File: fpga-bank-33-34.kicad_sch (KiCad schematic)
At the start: 1 part, among them U1 XC7K410T-2FFG900I

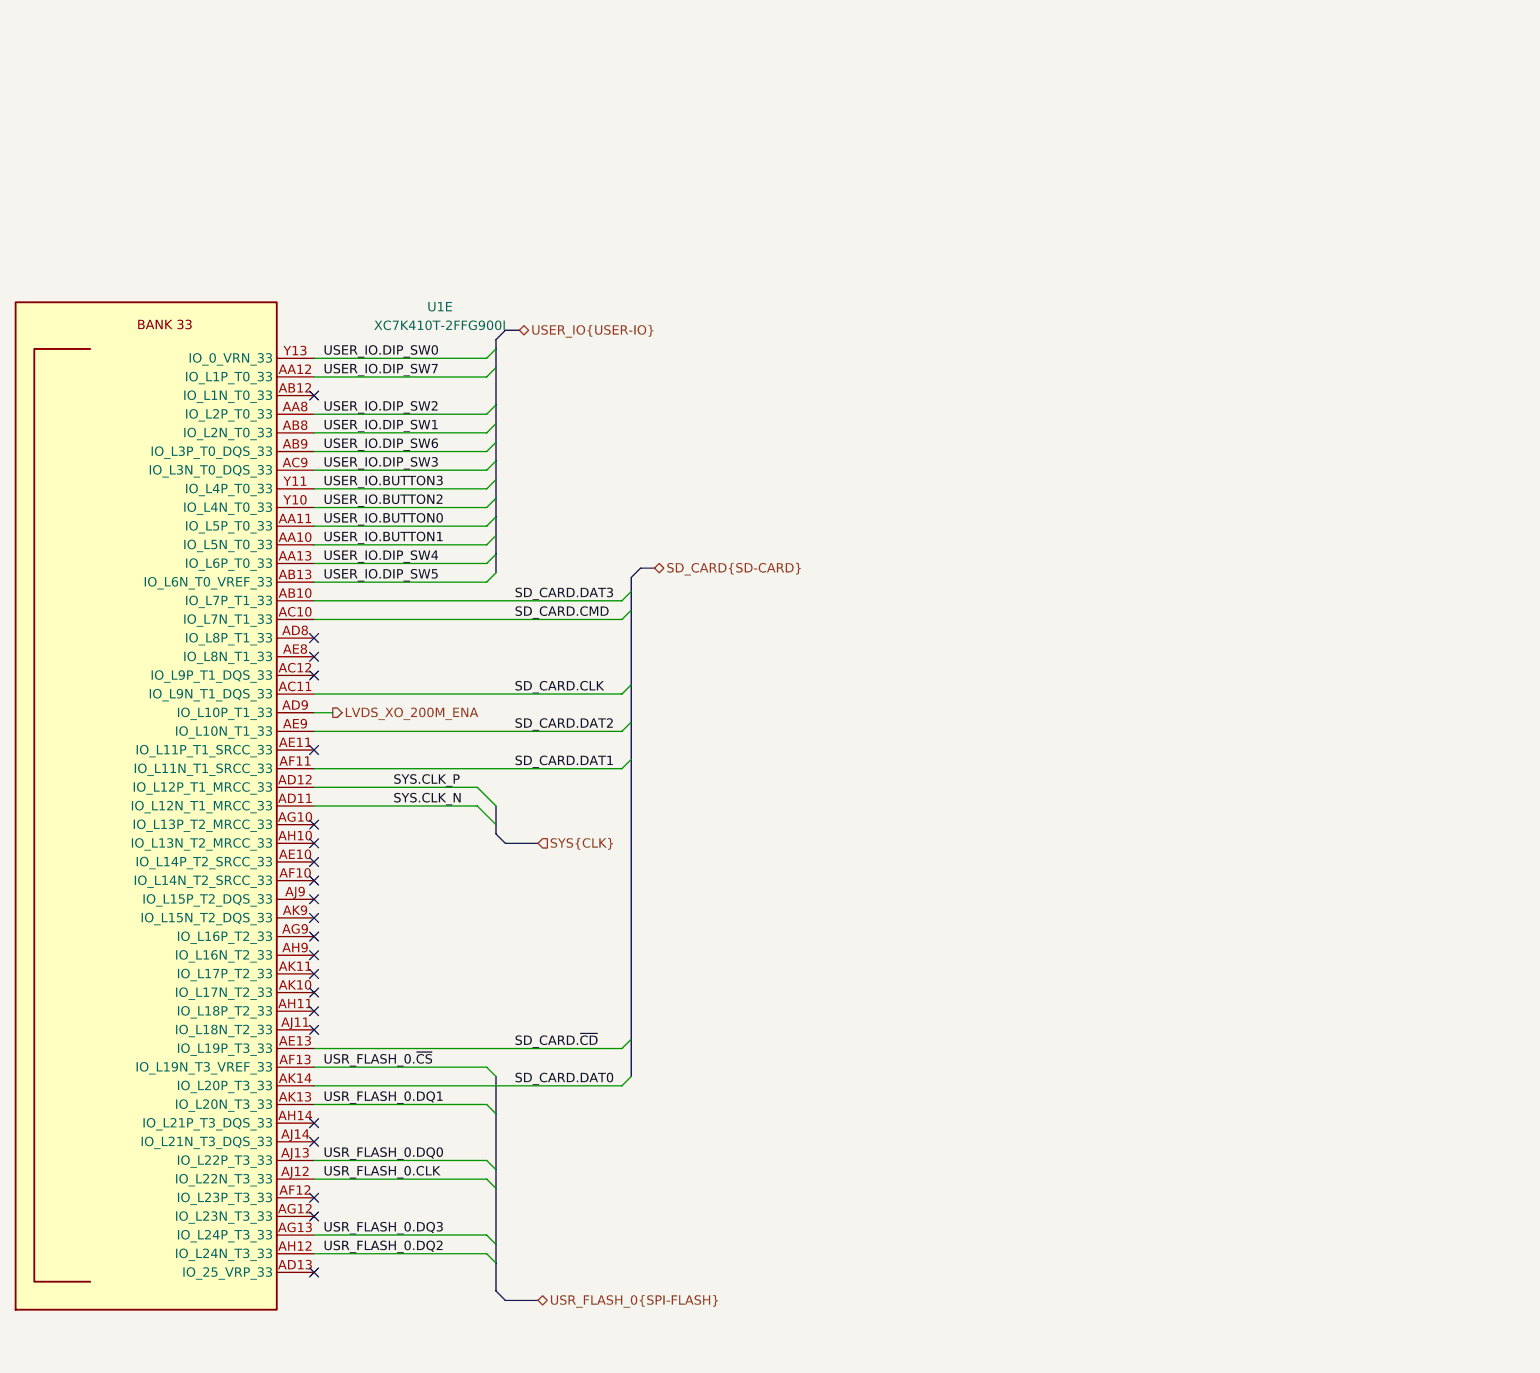
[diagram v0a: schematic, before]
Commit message: [#55729] Switch FPGA symbol to antmicroFPGAChips lib
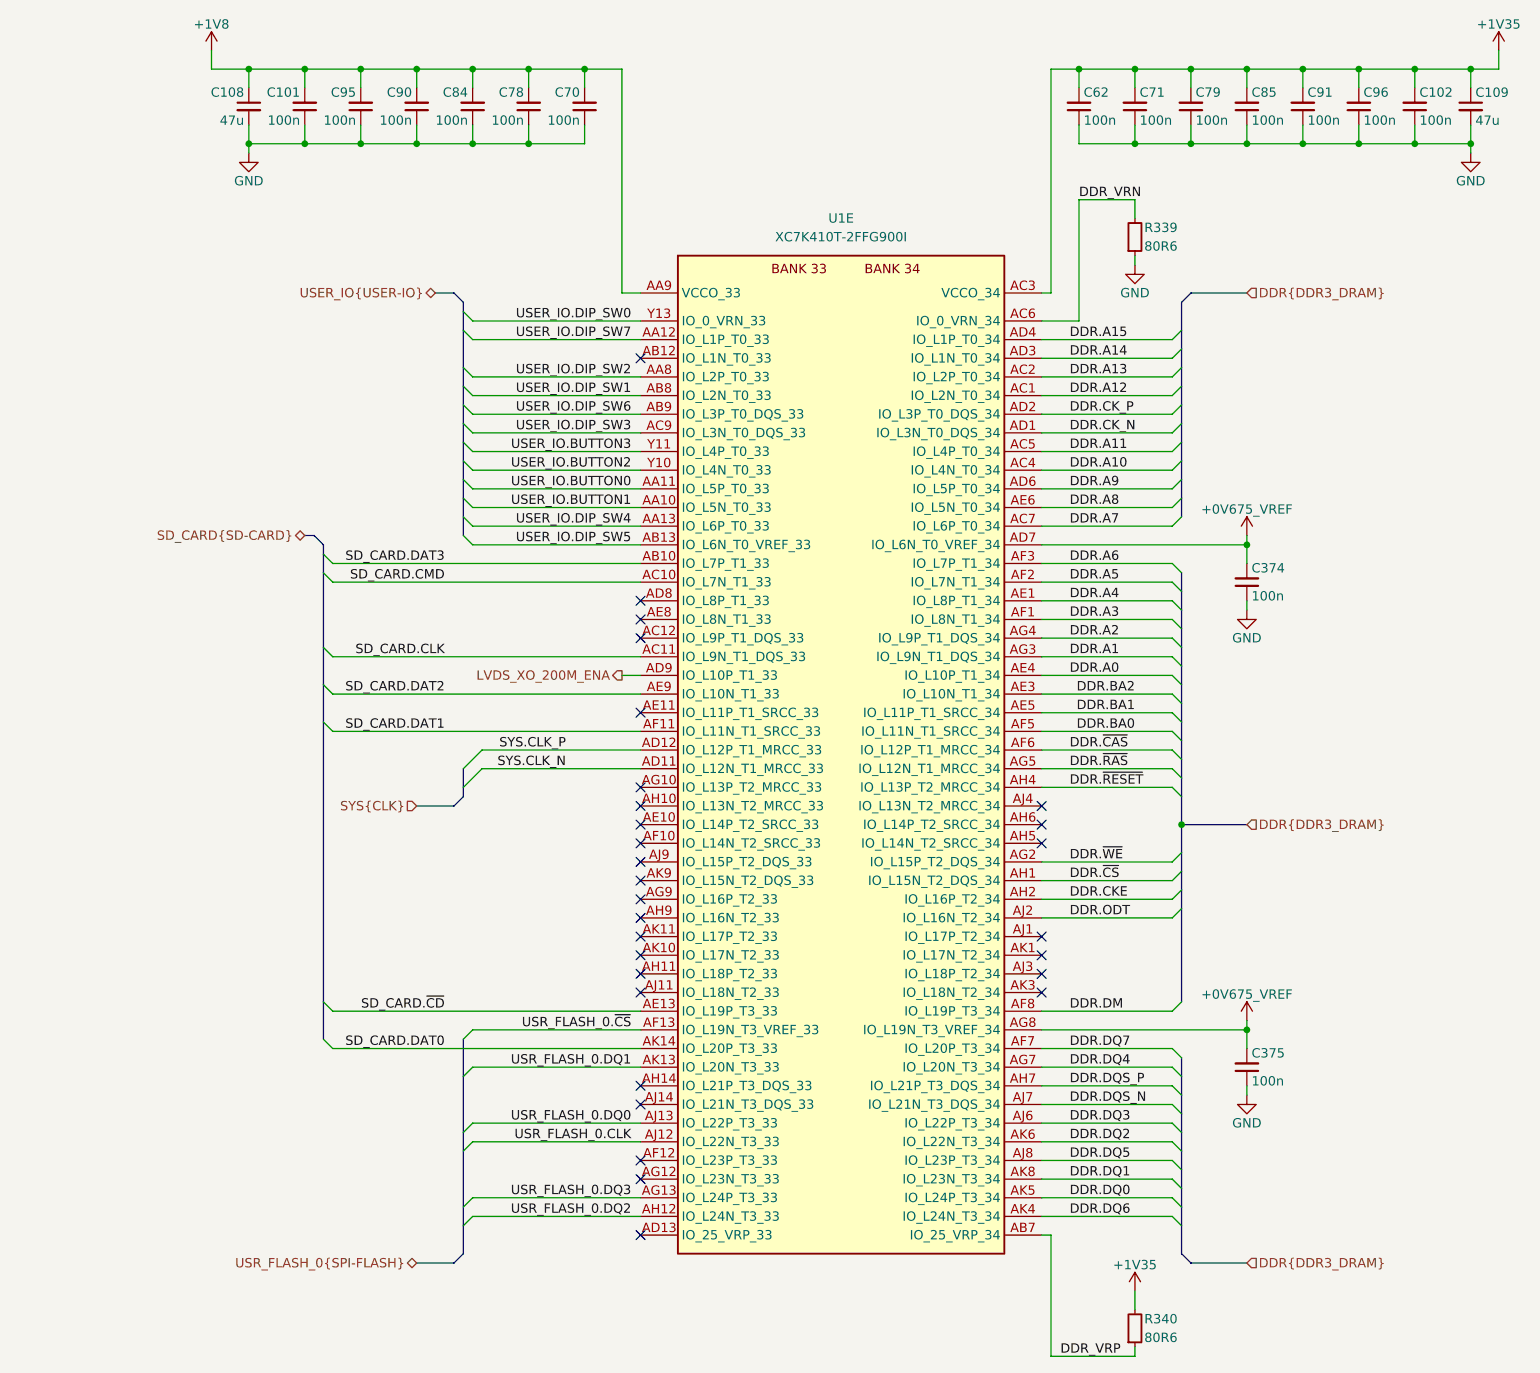
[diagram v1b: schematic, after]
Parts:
- added C101, C102, C374, C375, C62, C70, C71, C78, C79, C84, C85, C90, C91, C95, C96: C_100n_0402, antmicro-footprints:C_0402_1005Metric, symbol antmicroCapacitors0402:C_100n_0402
- added C108, C109: C_47u_0603, antmicro-footprints:C_0603_1608Metric, symbol antmicroCapacitors0603:C_47u_0603
- added R339, R340: R_80R6_0402_EIA, antmicro-footprints:R_0402_1005Metric_EIA, symbol antmicroResistors0402:R_80R6_0402_EIA
- U1: footprint K410T-devboard-footprints:xc7k410t-2ffg900I -> antmicro-footprints:BGA-900_31x31mm_Layout30x30_P1x1mm_FFG900; symbol K410T-devboard:XC7K410T-2FFG900I -> antmicroFPGAChips:XC7K410T-2FFG900I
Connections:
- new net +0V675_VREF: C374.2, C375.2, U1.AD7 (IO_L6N_T0_VREF_34), U1.AG8 (IO_L19N_T3_VREF_34)
- new net +1V35: C102.2, C109.1, C62.2, C71.2, C79.2, C85.2, C91.2, C96.2, R340.2, U1.AC3 (VCCO_34), U1.AE7 (VCCO_34), U1.AF4 (VCCO_34), U1.AG1 (VCCO_34), U1.AH8 (VCCO_34), U1.AJ5 (VCCO_34), U1.AK2 (VCCO_34)
- new net +1V8: C101.2, C108.1, C70.2, C78.2, C84.2, C90.2, C95.2, U1.AA9 (VCCO_33), U1.AC13 (VCCO_33), U1.AD10 (VCCO_33), U1.AG11 (VCCO_33), U1.AK12 (VCCO_33), U1.Y12 (VCCO_33)
- new net DDR.A0: U1.AE4 (IO_L10P_T1_34)
- new net DDR.A1: U1.AG3 (IO_L9N_T1_DQS_34)
- new net DDR.A10: U1.AC4 (IO_L4N_T0_34)
- new net DDR.A11: U1.AC5 (IO_L4P_T0_34)
- new net DDR.A12: U1.AC1 (IO_L2N_T0_34)
- new net DDR.A13: U1.AC2 (IO_L2P_T0_34)
- new net DDR.A14: U1.AD3 (IO_L1N_T0_34)
- new net DDR.A15: U1.AD4 (IO_L1P_T0_34)
- new net DDR.A2: U1.AG4 (IO_L9P_T1_DQS_34)
- new net DDR.A3: U1.AF1 (IO_L8N_T1_34)
- new net DDR.A4: U1.AE1 (IO_L8P_T1_34)
- new net DDR.A5: U1.AF2 (IO_L7N_T1_34)
- new net DDR.A6: U1.AF3 (IO_L7P_T1_34)
- new net DDR.A7: U1.AC7 (IO_L6P_T0_34)
- new net DDR.A8: U1.AE6 (IO_L5N_T0_34)
- new net DDR.A9: U1.AD6 (IO_L5P_T0_34)
- new net DDR.BA0: U1.AF5 (IO_L11N_T1_SRCC_34)
- new net DDR.BA1: U1.AE5 (IO_L11P_T1_SRCC_34)
- new net DDR.BA2: U1.AE3 (IO_L10N_T1_34)
- new net DDR.CKE: U1.AH2 (IO_L16P_T2_34)
- new net DDR.CK_N: U1.AD1 (IO_L3N_T0_DQS_34)
- new net DDR.CK_P: U1.AD2 (IO_L3P_T0_DQS_34)
- new net DDR.DM: U1.AF8 (IO_L19P_T3_34)
- new net DDR.DQ0: U1.AK5 (IO_L24P_T3_34)
- new net DDR.DQ1: U1.AK8 (IO_L23N_T3_34)
- new net DDR.DQ2: U1.AK6 (IO_L22N_T3_34)
- new net DDR.DQ3: U1.AJ6 (IO_L22P_T3_34)
- new net DDR.DQ4: U1.AG7 (IO_L20N_T3_34)
- new net DDR.DQ5: U1.AJ8 (IO_L23P_T3_34)
- new net DDR.DQ6: U1.AK4 (IO_L24N_T3_34)
- new net DDR.DQ7: U1.AF7 (IO_L20P_T3_34)
- new net DDR.DQS_N: U1.AJ7 (IO_L21N_T3_DQS_34)
- new net DDR.DQS_P: U1.AH7 (IO_L21P_T3_DQS_34)
- new net DDR.ODT: U1.AJ2 (IO_L16N_T2_34)
- new net DDR.~{CAS}: U1.AF6 (IO_L12P_T1_MRCC_34)
- new net DDR.~{CS}: U1.AH1 (IO_L15N_T2_DQS_34)
- new net DDR.~{RAS}: U1.AG5 (IO_L12N_T1_MRCC_34)
- new net DDR.~{RESET}: U1.AH4 (IO_L13P_T2_MRCC_34)
- new net DDR.~{WE}: U1.AG2 (IO_L15P_T2_DQS_34)
- new net DDR_VRN: R339.2, U1.AC6 (IO_0_VRN_34)
- new net DDR_VRP: R340.1, U1.AB7 (IO_25_VRP_34)
- new net GND: C101.1, C102.1, C108.2, C109.2, C374.1, C375.1, C62.1, C70.1, C71.1, C78.1, C79.1, C84.1, C85.1, C90.1, C91.1, C95.1, C96.1, R339.1
- no-connect marks 22 -> 29
